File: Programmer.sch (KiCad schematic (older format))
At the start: 71 parts, among them CON1 USB_OTG, M1 ESP-12E, P1 CONN_01X12, P3 CONN_12, Q1 BSS138L, Q2 MMBT3906, Q3 MMBT3904, Q4 BSS84, Q5 BSS138L, Q7 MMBT3904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

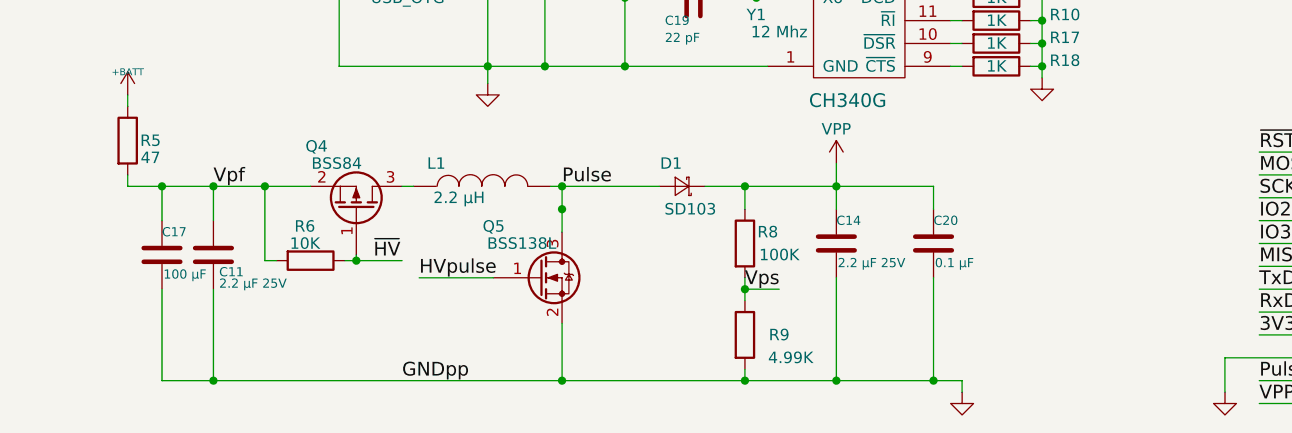
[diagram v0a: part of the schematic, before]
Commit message: Small change to Voltage Boost Circuit (Hardware V00I)
Added a loading resistor and another filter capacitor to the Voltage
boost Circuit. R26 and C23
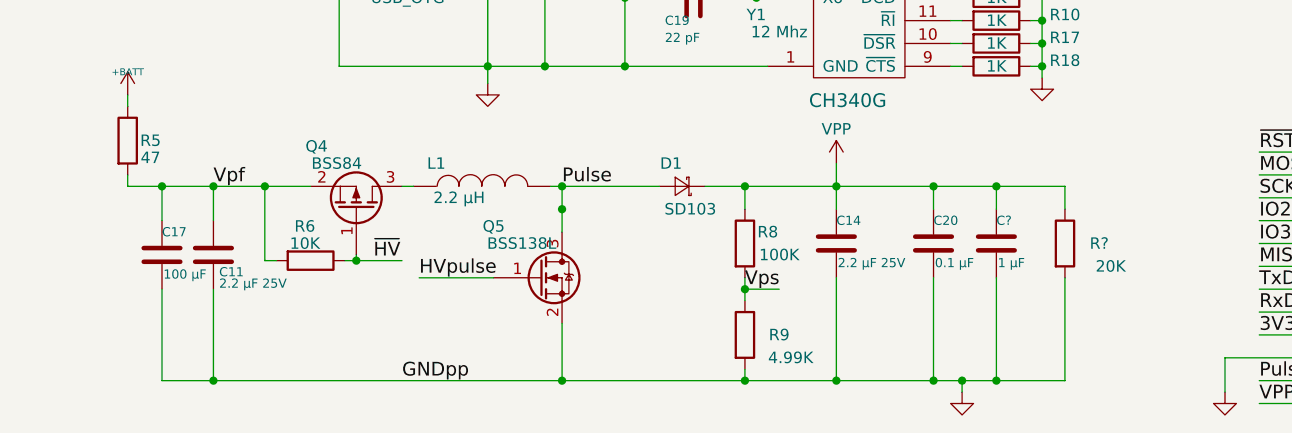
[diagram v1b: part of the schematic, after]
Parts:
- added C?: 1 µF, Capacitors_SMD:C_1206, symbol C
- added R?: 20K, Resistors_SMD:R_1206, symbol R
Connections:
- wire segments 269 -> 273
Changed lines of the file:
@@
 Connection ~ 3300 6850
 Wire Wire Line
-	3925 6750 4925 6750
+	3925 6750 5500 6750
 Wire Wire Line
 	4100 6750 4100 6850
@@
 	4100 7200 4250 7200
 Wire Wire Line
-	1550 7600 5050 7600
+	1550 7600 5500 7600
 $Comp
 L Q_NMOS_GSD Q5
@@
 Wire Wire Line
 	4500 3975 4500 4525
+$Comp
+L C C?
+U 1 1 57EE9507
+P 5200 7000
+F 0 "C?" H 5200 7100 40  0000 L CNN
+F 1 "1 µF" H 5206 6915 40  0000 L CNN
+F 2 "Capacitors_SMD:C_1206" H 5238 6850 30  0001 C CNN
+F 3 "~" H 5200 7000 60  0000 C CNN
+	1    5200 7000
+	1    0    0    -1
+$EndComp
+$Comp
+L R R?
+U 1 1 57EE95E9
+P 5500 7000
+F 0 "R?" H 5650 7000 50  0000 C CNN
+F 1 "20K" H 5700 6900 50  0000 C CNN
+F 2 "Resistors_SMD:R_1206" V 5430 7000 30  0001 C CNN
+F 3 "" H 5500 7000 30  0000 C CNN
+	1    5500 7000
+	1    0    0    -1
+$EndComp
+Wire Wire Line
+	5200 7600 5200 7150
+Connection ~ 5050 7600
+Wire Wire Line
+	5500 7600 5500 7150
+Connection ~ 5200 7600
+Wire Wire Line
+	5200 6750 5200 6850
+Connection ~ 4925 6750
+Wire Wire Line
+	5500 6750 5500 6850
+Connection ~ 5200 6750
 $EndSCHEMATC

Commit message: New Layout Hardware V00I
Updated layout to match schematic in Version H. Ready to go to
fabrication.
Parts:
- removed U3: TXS0108EPWR, Housings_SSOP:TSSOP-20_4.4x6.5mm_Pitch0.65mm, symbol TXB0108PWR
- added U3: TXS0108PWR, Housings_SSOP:TSSOP-20_4.4x6.5mm_Pitch0.65mm, symbol TXS0108PWR
- gave numbers to parts that had none: 2
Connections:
- net labels removed: SCK
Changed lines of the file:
@@
 ~RST
 Text Label 6350 6800 0    60   ~ 0
-SCK
+SCLK
 Text Label 6800 3025 0    60   ~ 0
 IO2
@@
 Wire Wire Line
 	6550 2225 6500 2225
-$Comp
-L TXB0108PWR U3
-U 1 1 57E51A7C
-P 8950 3125
-F 0 "U3" H 8650 4025 59  0000 C CNN
-F 1 "TXS0108EPWR" H 8900 3925 59  0000 C CNN
-F 2 "Housings_SSOP:TSSOP-20_4.4x6.5mm_Pitch0.65mm" H 9000 3125 59  0001 C CNN
-F 3 "" H 9000 3125 59  0001 C CNN
-	1    8950 3125
-	1    0    0    -1
-$EndComp
 Wire Wire Line
 	9925 2425 10575 2425
@@
 	4500 3975 4500 4525
 $Comp
-L C C?
+L C C23
 U 1 1 57EE9507
 P 5200 7000
-F 0 "C?" H 5200 7100 40  0000 L CNN
+F 0 "C23" H 5200 7100 40  0000 L CNN
 F 1 "1 µF" H 5206 6915 40  0000 L CNN
 F 2 "Capacitors_SMD:C_1206" H 5238 6850 30  0001 C CNN
@@
 $EndComp
 $Comp
-L R R?
+L R R26
 U 1 1 57EE95E9
 P 5500 7000
-F 0 "R?" H 5650 7000 50  0000 C CNN
+F 0 "R26" H 5650 7000 50  0000 C CNN
 F 1 "20K" H 5700 6900 50  0000 C CNN
 F 2 "Resistors_SMD:R_1206" V 5430 7000 30  0001 C CNN
@@
 	5500 6750 5500 6850
 Connection ~ 5200 6750
+$Comp
+L TXS0108PWR U3
+U 1 1 57F81A8D
+P 8950 3125
+F 0 "U3" H 8650 4025 59  0000 C CNN
+F 1 "TXS0108PWR" H 8900 3925 59  0000 C CNN
+F 2 "Housings_SSOP:TSSOP-20_4.4x6.5mm_Pitch0.65mm" H 9000 3125 59  0001 C CNN
+F 3 "" H 9000 3125 59  0001 C CNN
+	1    8950 3125
+	1    0    0    -1
+$EndComp
 $EndSCHEMATC

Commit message: Fixed errors found Hardware V00J
Fixed DTR/RTS Lines and my logo on the board
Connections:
- net at Q7.2 (E), R20.2: now also U8.14 (~RTS); no longer U8.13 (~DTR)
- net at Q8.2 (E), R19.2: now also U8.13 (~DTR); no longer U8.14 (~RTS)
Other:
- note removed: "Test before next board spin"
- moved on the sheet: Q7, Q8, R19, R20
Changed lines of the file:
@@
 Text Label 4875 2225 0    60   ~ 0
 ~RST
-Text Label 6175 4850 0    60   ~ 0
+Text Label 6150 5900 0    60   ~ 0
 ~RST
 Wire Wire Line
@@
 Connection ~ 9450 2425
 Wire Wire Line
-	6550 2225 6550 5900
-Wire Wire Line
 	6500 2325 6700 2325
 Wire Wire Line
@@
 L R R19
 U 1 1 56C810B9
-P 5550 5100
-F 0 "R19" V 5400 5075 50  0000 C CNN
-F 1 "10K" V 5475 5075 50  0000 C CNN
-F 2 "Resistors_SMD:R_1206" V 5480 5100 30  0001 C CNN
-F 3 "" H 5550 5100 30  0000 C CNN
-	1    5550 5100
+P 5550 5650
+F 0 "R19" V 5400 5625 50  0000 C CNN
+F 1 "10K" V 5475 5625 50  0000 C CNN
+F 2 "Resistors_SMD:R_1206" V 5480 5650 30  0001 C CNN
+F 3 "" H 5550 5650 30  0000 C CNN
+	1    5550 5650
 	0    1    1    0
 $EndComp
@@
 L MMBT3904 Q7
 U 1 1 56C81360
-P 5950 5100
-F 0 "Q7" H 6150 5175 50  0000 L CNN
-F 1 "MMBT3904" H 6150 5100 50  0000 L CNN
-F 2 "TO_SOT_Packages_SMD:SOT-23" H 6150 5025 50  0001 L CIN
-F 3 "" H 5950 5100 50  0000 L CNN
-	1    5950 5100
-	1    0    0    -1
-$EndComp
-$Comp
-L MMBT3904 Q8
-U 1 1 56C816B2
 P 5950 5650
-F 0 "Q8" H 6150 5725 50  0000 L CNN
+F 0 "Q7" H 6150 5725 50  0000 L CNN
 F 1 "MMBT3904" H 6150 5650 50  0000 L CNN
 F 2 "TO_SOT_Packages_SMD:SOT-23" H 6150 5575 50  0001 L CIN
@@
 $EndComp
 $Comp
+L MMBT3904 Q8
+U 1 1 56C816B2
+P 5950 5100
+F 0 "Q8" H 6150 5175 50  0000 L CNN
+F 1 "MMBT3904" H 6150 5100 50  0000 L CNN
+F 2 "TO_SOT_Packages_SMD:SOT-23" H 6150 5025 50  0001 L CIN
+F 3 "" H 5950 5100 50  0000 L CNN
+	1    5950 5100
+	1    0    0    -1
+$EndComp
+$Comp
 L R R20
 U 1 1 56C81DE2
-P 5550 5650
-F 0 "R20" V 5400 5625 50  0000 C CNN
-F 1 "10K" V 5475 5625 50  0000 C CNN
-F 2 "Resistors_SMD:R_1206" V 5480 5650 30  0001 C CNN
-F 3 "" H 5550 5650 30  0000 C CNN
-	1    5550 5650
+P 5550 5100
+F 0 "R20" V 5400 5075 50  0000 C CNN
+F 1 "10K" V 5475 5075 50  0000 C CNN
+F 2 "Resistors_SMD:R_1206" V 5480 5100 30  0001 C CNN
+F 3 "" H 5550 5100 30  0000 C CNN
+	1    5550 5100
 	0    1    1    0
 $EndComp
@@
 	6050 4900 6050 4850
 Wire Wire Line
-	6050 4850 6325 4850
-Wire Wire Line
-	6550 5900 6050 5900
+	6050 5900 6325 5900
 Wire Wire Line
 	6050 5900 6050 5850
@@
 	7400 4525 7400 3225
 Connection ~ 7400 3225
-Text Notes 975  2425 0    79   ~ 16
-Test before next board spin
 Wire Wire Line
 	6550 3900 5175 3900
@@
 	1    0    0    -1
 $EndComp
+Wire Wire Line
+	6550 2225 6550 4850
+Wire Wire Line
+	6550 4850 6050 4850
 $EndSCHEMATC

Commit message: Hardware V00K
Removed SPI RAM, Switched to HSPI only. Using FAN5331 for switching
regulator.  Some cleanup and re-labeling
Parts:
- removed Q4: BSS84, TO_SOT_Packages_SMD:SOT-23, symbol Q_PMOS_GSD
- removed Q5: BSS138L, TO_SOT_Packages_SMD:SOT-23, symbol Q_NMOS_GSD
- removed U2: 23LC1024, Housings_SOIC:SOIC-8_3.9x4.9mm_Pitch1.27mm, symbol 23LC1024
- added L2: 10 µH, Choke_SMD:Choke_SMD_1206_Standard, symbol INDUCTOR
- added Q4: MMBT3904, TO_SOT_Packages_SMD:SOT-23, symbol MMBT3904
- added R27: 10K, symbol R
- added U2: FAN5331, SOT-23-5, symbol LM2731XMF
- C5: value 0.1 µF -> C; footprint Capacitors_SMD:C_1206 -> (none)
- CON1: symbol USB_OTG -> USB_OTG-RESCUE-Programmer
- L1: value 2.2 µH -> 10 µH
- R15: value 1M -> 100K
- R26: value 20K -> 4.99K
- R6: value 10K -> R; footprint Resistors_SMD:R_1206 -> (none)
- R8: value 100K -> 150K
- R9: value 4.99K -> 100K; footprint Resistors_SMD:R_1206 -> (none)
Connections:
- net labels added: HV, H_CS
- net labels removed: IO2, IO3, Pulse, ~HV
- wire segments 273 -> 256
- no-connect marks 2 -> 8
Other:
- note added: "19.68 Volts Maximum"
- note removed: "The level shifter needs tested."
- moved on the sheet: C10, C11, C12, C13, C14, C17, C18, C19, C20, C23, C3, CON1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

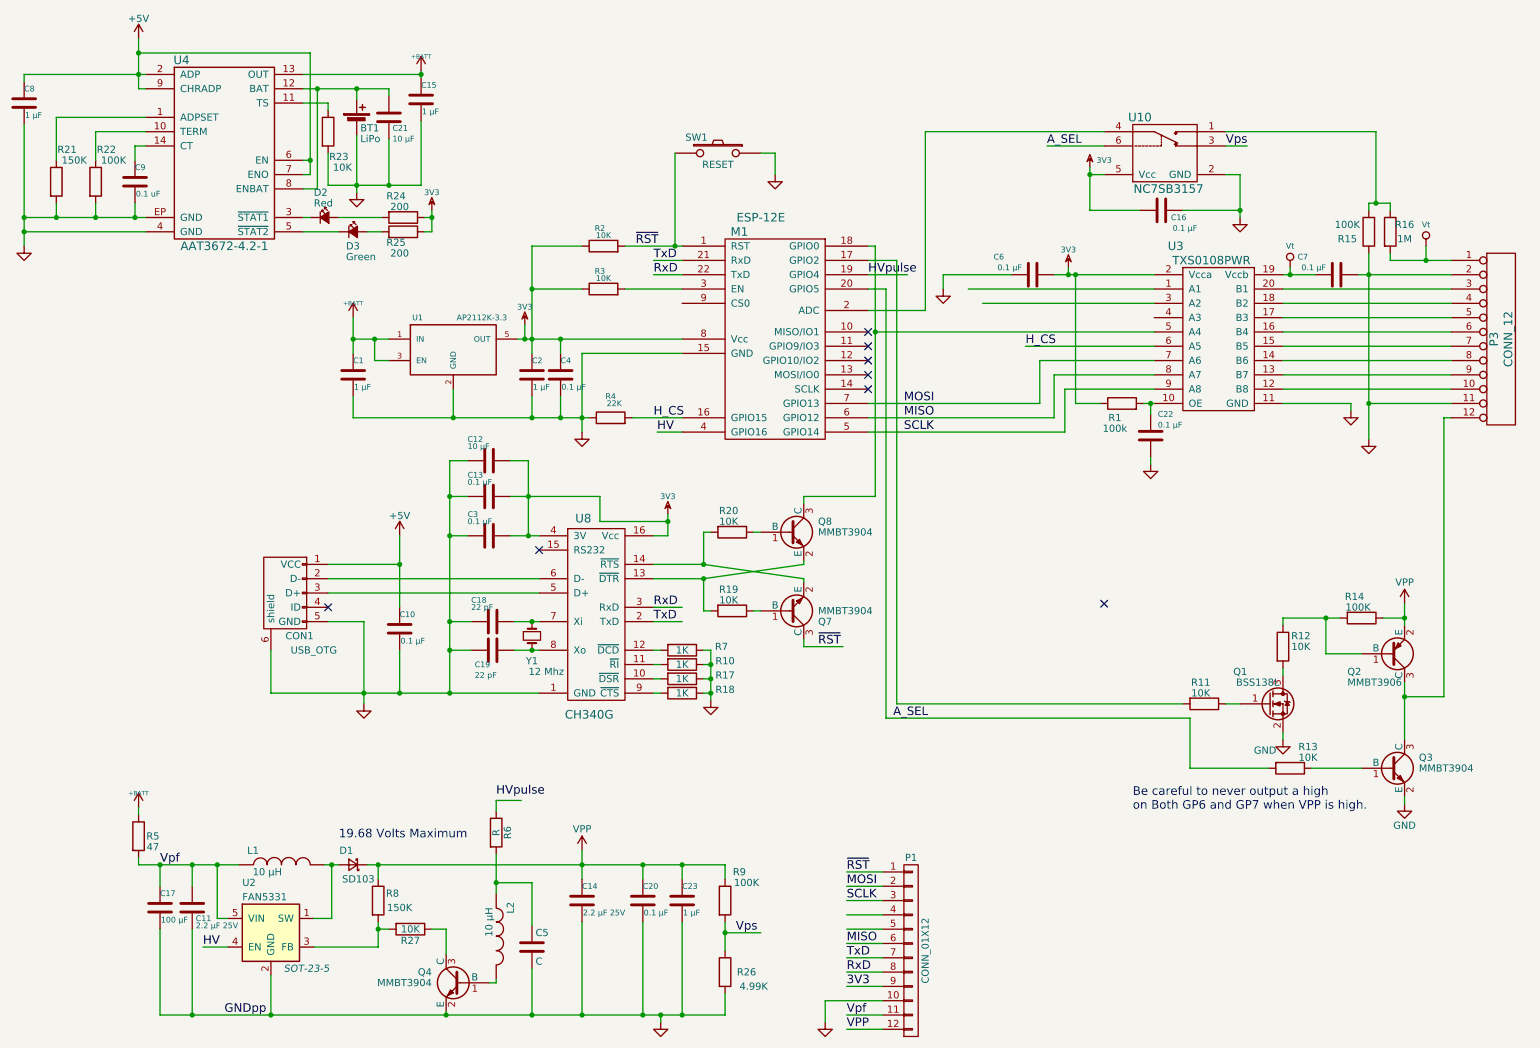
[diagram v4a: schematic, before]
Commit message: Multiple Level shifters instead of one
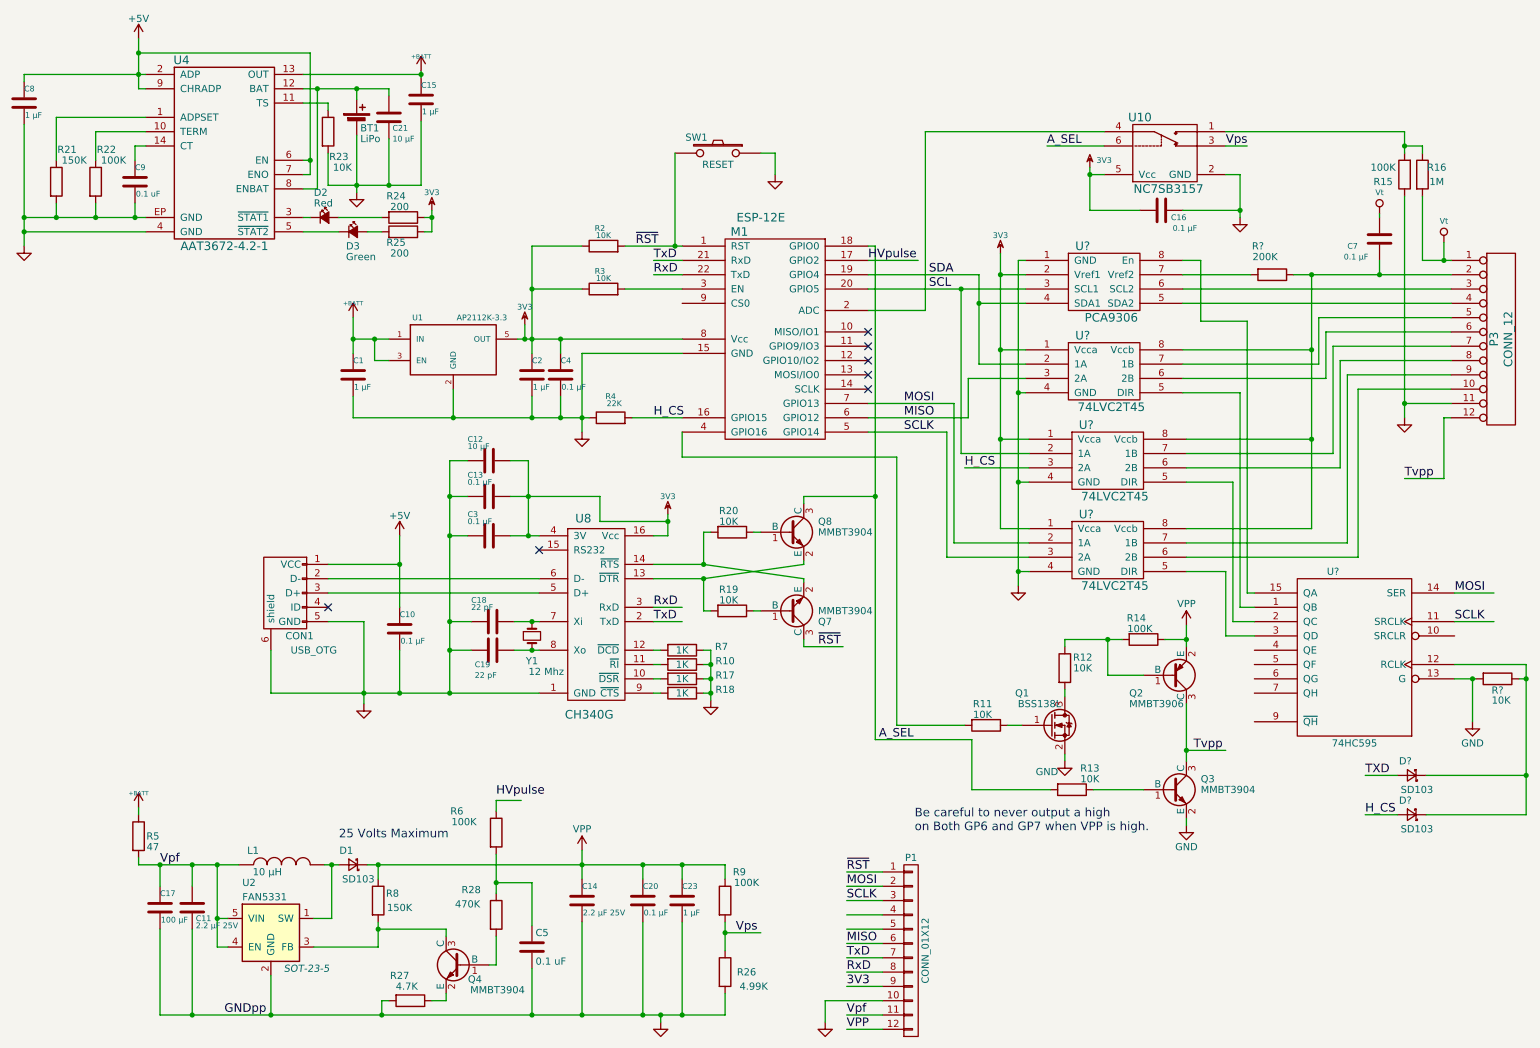
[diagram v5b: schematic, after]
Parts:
- removed C22, C6: 0.1 µF, Capacitors_SMD:C_1206, symbol C
- removed L2: 10 µH, Choke_SMD:Choke_SMD_1206_Standard, symbol INDUCTOR
- removed R1: 100k, Resistors_SMD:R_1206, symbol R
- removed U3: TXS0108PWR, Housings_SSOP:TSSOP-20_4.4x6.5mm_Pitch0.65mm, symbol TXS0108PWR
- added D? (x2): SD103, Diodes_SMD:SOD-323, symbol D_Schottky_Small
- added R28: 470K, symbol R
- added R?: 200K, symbol R
- added R?: 10K, symbol R
- added U? (x3): 74LVC2T45, symbol 74LVC2T45
- added U?: PCA9306, symbol PCA9306
- added U?: 74HC595, symbol 74HC595
- C5: value C -> 0.1 uF
- R27: value 10K -> 4.7K
- R6: value R -> 100K
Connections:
- net labels added: SCL, SDA, TXD, Tvpp
- net labels removed: HV
- wire segments 256 -> 301
- no-connect marks 8 -> 7
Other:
- note added: "25 Volts Maximum"
- note removed: "19.68 Volts Maximum"
- moved on the sheet: C7, Q1, Q2, Q3, Q4, R11, R12, R13, R14, R15, R16
